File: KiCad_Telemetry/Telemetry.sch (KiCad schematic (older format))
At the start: 42 parts, among them J1 USB_A to Computer, J2 Conn_ARM_JTAG_SWD_10, J3 3.3 V Connectors, J5 5V Connectors, SW1 Reset Button, U1 NRF24L01_Breakout, U2 STM32F042C6T7, U3 AZ1117-3.3, Y1 8 MHz

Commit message: Initial STM32 project commit
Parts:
- removed D10, D11, D5, D6, D7, D8, D9: LED, symbol Device:LED
- removed R3, R4, R5, R6, R7, R8, R9: 65, symbol Device:R
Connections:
- wire segments 131 -> 110

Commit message: Updated the schematic
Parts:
- removed J2: Conn_ARM_JTAG_SWD_10, symbol Connector:Conn_ARM_JTAG_SWD_10
- removed U3: AZ1117-3.3, symbol Regulator_Linear:AZ1117-3.3
- removed U?: SN65HVD230, Package_SO:SOIC-8_3.9x4.9mm_P1.27mm, symbol Interface_CAN_LIN:SN65HVD230
- added C1: Opt. Decoupling Cap, Capacitor_SMD:C_0603_1608Metric_Pad1.05x0.95mm_HandSolder, symbol Device:C_Small
- added J2: Conn_01x05, Connector_PinHeader_2.54mm:PinHeader_1x05_P2.54mm_Vertical, symbol Connector_Generic:Conn_01x05
- added J6: Conn_01x07, symbol Connector_Generic:Conn_01x07
- added U3: TLV70033_SOT23-5, Package_TO_SOT_SMD:SOT-23-5, symbol Regulator_Linear:TLV70033_SOT23-5
- added U4: TPS7A7001DDA, Package_SO:TI_SO-PowerPAD-8, symbol Regulator_Linear:TPS7A7001DDA
- 0.1uF1, C2, C3, C4, C5, C7: footprint (none) -> Capacitor_SMD:C_0603_1608Metric_Pad1.05x0.95mm_HandSolder
- 100nF1: renamed from 100nF; footprint (none) -> Capacitor_SMD:C_0603_1608Metric_Pad1.05x0.95mm_HandSolder
- C6: value 22uF -> 1uF; footprint (none) -> Capacitor_SMD:C_0603_1608Metric_Pad1.05x0.95mm_HandSolder
- C8: value 10uF -> 1uF; footprint (none) -> Capacitor_SMD:C_0603_1608Metric_Pad1.05x0.95mm_HandSolder
- D1, D2: footprint (none) -> LED_SMD:LED_0603_1608Metric_Pad1.05x0.95mm_HandSolder
- D3, D4: footprint (none) -> Diode_SMD:D_0603_1608Metric_Pad1.05x0.95mm_HandSolder
- J1: footprint (none) -> Connector_USB:USB_A_CNCTech_1001-011-01101_Horizontal; MouserNO (none) -> 530-SS-52100-001; UnitPrice (none) -> 0,387
- R1, R2: footprint (none) -> Resistor_SMD:R_0603_1608Metric_Pad1.05x0.95mm_HandSolder
- R3, R4: renamed from R?; footprint (none) -> Resistor_SMD:R_0603_1608Metric_Pad1.05x0.95mm_HandSolder
- U2: footprint (none) -> Package_QFP:LQFP-48-1EP_7x7mm_P0.5mm_EP3.6x3.6mm; MouserNO (none) -> 511-STM32F042C6T7; UnitPrice (none) -> 2,75
- Y1: footprint (none) -> Crystal:Crystal_HC49-4H_Vertical
- gave numbers to parts that had none: 1
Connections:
- wire segments 110 -> 123
- no-connect marks 23 -> 20
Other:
- note added: "Determine CAN IC"
- note added: "Possibly peak 48 Volt input voltage rail in car"
- note added: "Unable to design solution until Mechanical choose Tires\n\nCurrent solution: SPI Connection for external board, similar to the NRF24"
- note removed: "2.4 GHZ or 433 MHz ?"
- note removed: "3.3V Rail; Stable or not? How do we reduce voltage ripple?"
- note removed: "Determine IC for this"
- note removed: "Does the car already have a solution?"
- note removed: "FSK?"
- note removed: "Suggested solution:\n- Purchase TPMS solution for wheels\n- Spy with RTLSDR\n- Purchase receiver module with demodulation\n- Fit on to board."
- note removed: "What Modulation is used?"
- moved on the sheet: C6

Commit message: Completed footprint allocation and BOM
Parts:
- removed R3, R4: R, Resistor_SMD:R_0603_1608Metric_Pad1.05x0.95mm_HandSolder, symbol Device:R
- removed SW1: Reset Button, symbol Switch:SW_Push
- removed U4: TPS7A7001DDA, Package_SO:TI_SO-PowerPAD-8, symbol Regulator_Linear:TPS7A7001DDA
- added C10: Opt. Decoupling Cap, Capacitor_SMD:C_0603_1608Metric_Pad1.05x0.95mm_HandSolder, symbol Device:C_Small
- added IC1: TCAN1044VDRQ1, SOIC127P600X175-8N, symbol TCAN1044VDRQ1:TCAN1044VDRQ1
- added S1: B3F-4000, B3F-4000, symbol B3F-4000:B3F-4000
- C11: renamed from 0.1uF1; value C_Small -> 0.1 uF
- C9: renamed from 100nF1; value C_Small -> 100nF
- D1, D2: MouserNO (none) -> 720-KRDELPS122A5163; UnitPrice (none) -> 0,369 €
- J1: Description (none) -> USB Connection for 5V Supply and PC Communication
- J3, J4, J5: footprint (none) -> TerminalBlock_Phoenix:TerminalBlock_Phoenix_MKDS-1,5-2_1x02_P5.00mm_Horizontal; MouserNO (none) -> 651-1934861; UnitPrice (none) -> 0,387 €
- J6: footprint (none) -> Connector_PinSocket_1.00mm:PinSocket_1x07_P1.00mm_Vertical
- R1: value 65 -> 55
- R2: value R -> 55
- U1: Description (none) -> NRF24 Breakout board connection: Board purchased seperately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
- U2: Description (none) -> STM32 Processor; USB, CAN, UART, SPI Comms.
- U3: Description (none) -> 5V to 3.3V Linear regulator
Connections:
- net labels added: CAN_STB
- wire segments 123 -> 129
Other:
- note added: "All LED's assume Vf = 2.2 V , If = 20 mA"
- note removed: "All LED's assume Vf = 2 V , If = 20 mA"
- note removed: "Determine CAN IC"
- note removed: "IS CAN 5V or 3.3 V?"
- moved on the sheet: C11, J4, J5

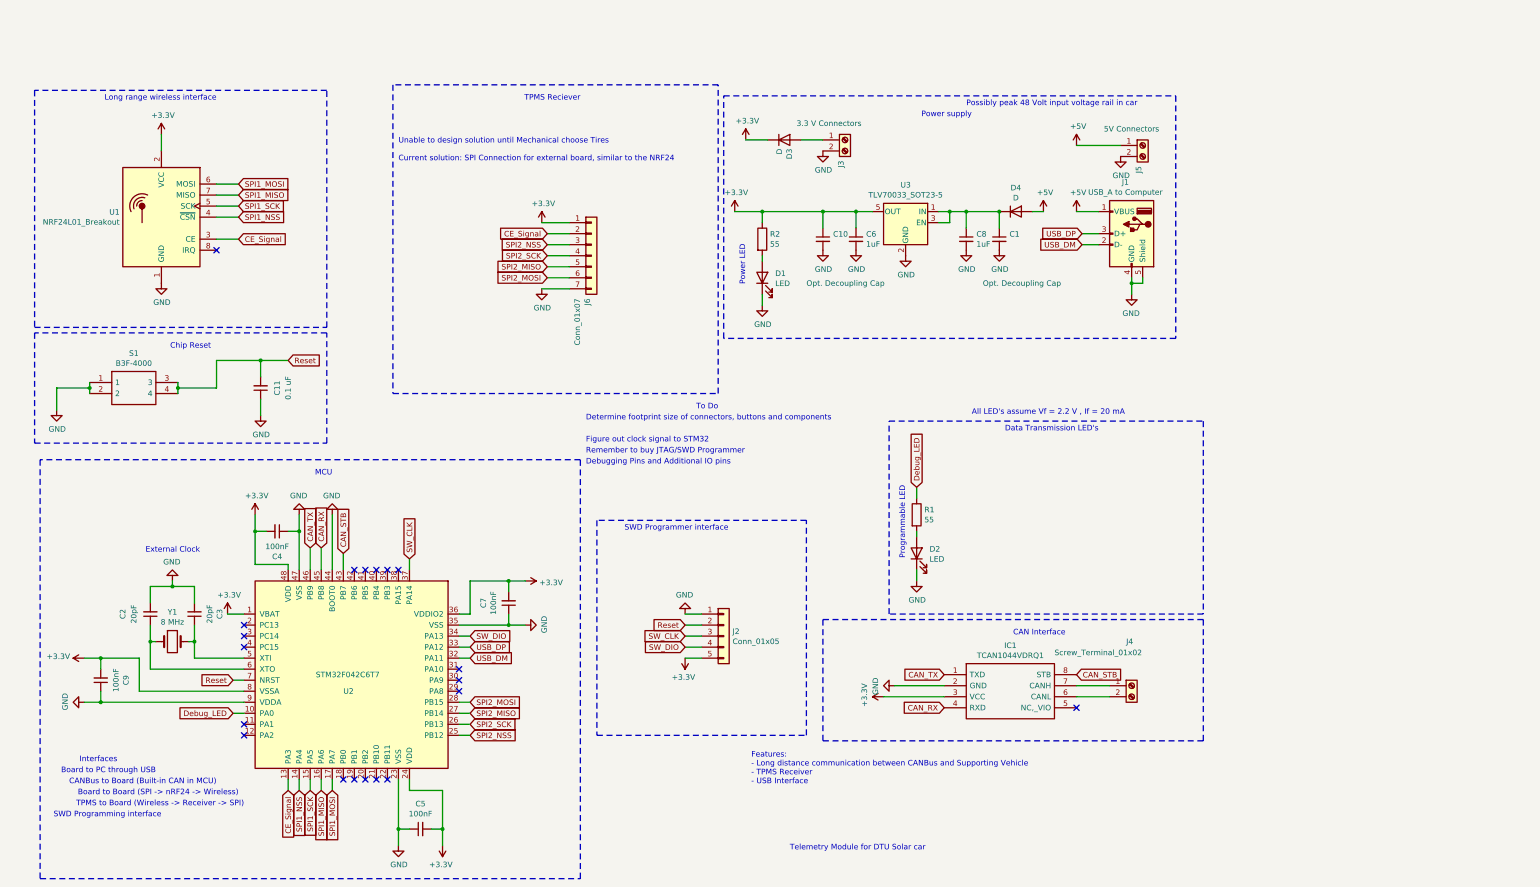
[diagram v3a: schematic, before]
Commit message: Finished intial CAN-FD KiCad Design. Awaiting peer review
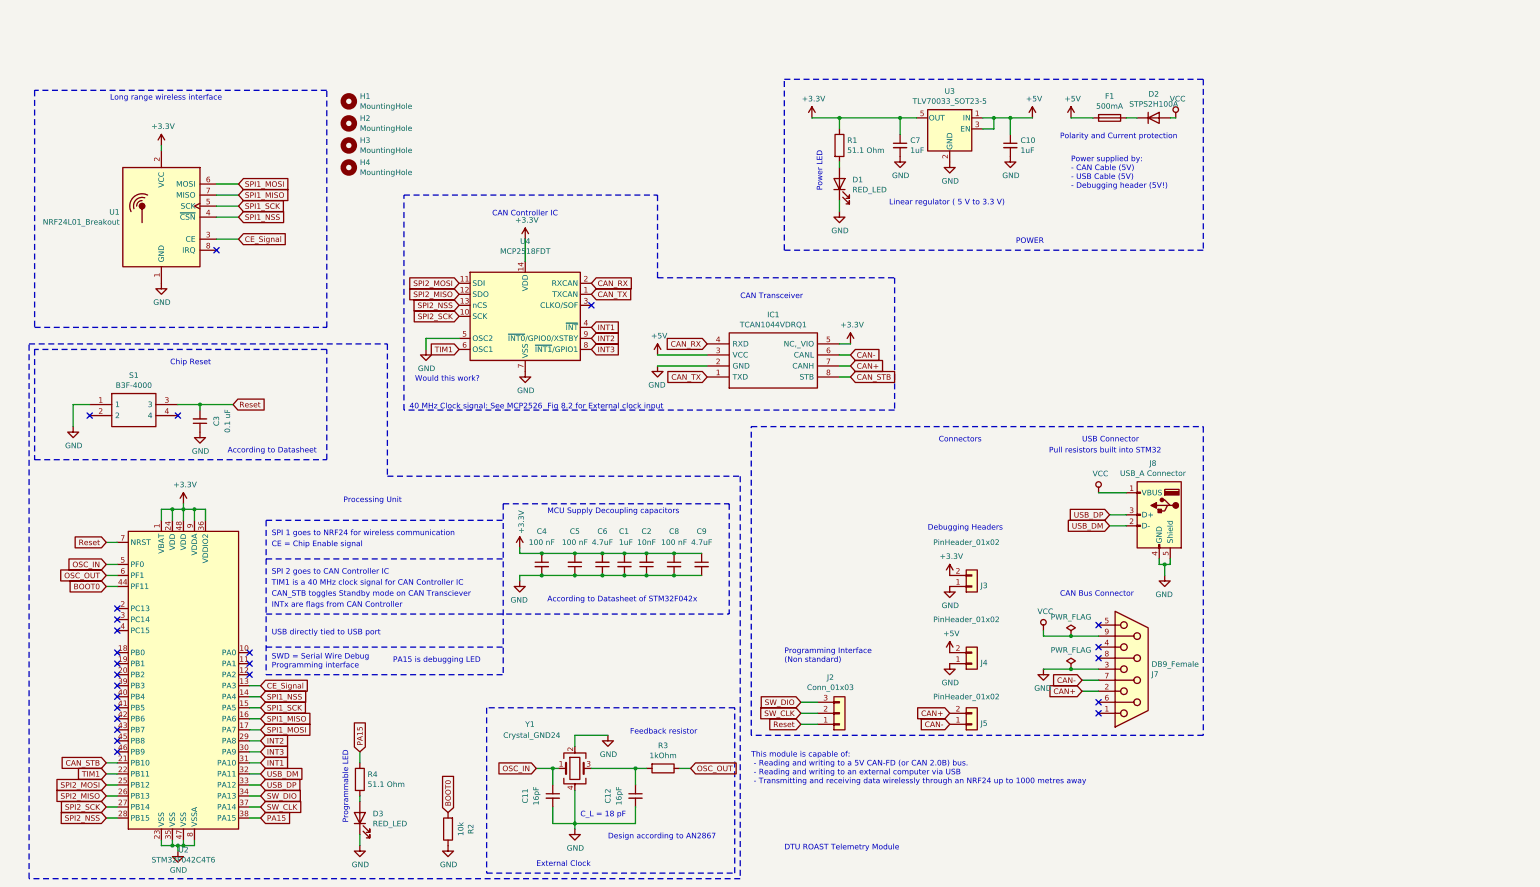
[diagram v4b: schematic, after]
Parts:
- removed C2, C3: 20pF, Capacitor_SMD:C_0603_1608Metric_Pad1.05x0.95mm_HandSolder, symbol Device:C_Small
- removed D3: D, Diode_SMD:D_0603_1608Metric_Pad1.05x0.95mm_HandSolder, symbol Device:D
- removed J2: Conn_01x05, Connector_PinHeader_2.54mm:PinHeader_1x05_P2.54mm_Vertical, symbol Connector_Generic:Conn_01x05
- removed J3: 3.3 V Connectors, TerminalBlock_Phoenix:TerminalBlock_Phoenix_MKDS-1,5-2_1x02_P5.00mm_Horizontal, symbol Connector:Screw_Terminal_01x02
- removed J4: Screw_Terminal_01x02, TerminalBlock_Phoenix:TerminalBlock_Phoenix_MKDS-1,5-2_1x02_P5.00mm_Horizontal, symbol Connector:Screw_Terminal_01x02
- removed J5: 5V Connectors, TerminalBlock_Phoenix:TerminalBlock_Phoenix_MKDS-1,5-2_1x02_P5.00mm_Horizontal, symbol Connector:Screw_Terminal_01x02
- removed J6: Conn_01x07, Connector_PinSocket_1.00mm:PinSocket_1x07_P1.00mm_Vertical, symbol Connector_Generic:Conn_01x07
- removed U2: STM32F042C6T7, Package_QFP:LQFP-48-1EP_7x7mm_P0.5mm_EP3.6x3.6mm, symbol stm32f042c6t7:STM32F042C6T7
- removed Y1: 8 MHz, Crystal:Crystal_HC49-4H_Vertical, symbol Device:Crystal
- added C11, C12: 16pF, Capacitor_SMD:C_0402_1005Metric, symbol Device:C_Small
- added C9: 4.7uF, Capacitor_SMD:C_0402_1005Metric, symbol Device:C_Small
- added F1: 500mA, Fuse:Fuse_0603_1608Metric_Pad1.05x0.95mm_HandSolder, symbol Device:Fuse
- added H1, H2, H3, H4: MountingHole, MountingHole:MountingHole_3.5mm, symbol Mechanical:MountingHole
- added J2: Conn_01x03, Connector_PinHeader_2.54mm:PinHeader_1x03_P2.54mm_Vertical, symbol Connector_Generic:Conn_01x03
- added J3, J4, J5: PinHeader_01x02, Connector_PinHeader_2.54mm:PinHeader_1x02_P2.54mm_Vertical, symbol Connector_Generic:Conn_01x02
- added J7: DB9_Female, Connector_Dsub:DSUB-9_Female_Horizontal_P2.77x2.84mm_EdgePinOffset4.94mm_Housed_MountingHolesOffset7.48mm, symbol Connector:DB9_Female
- added R3: 1kOhm, Resistor_SMD:R_0402_1005Metric, symbol Device:R
- added R4: 51.1 Ohm, Resistor_SMD:R_0603_1608Metric_Pad1.05x0.95mm_HandSolder, symbol Device:R
- added U2: STM32F042C4T6, Package_QFP:LQFP-48_7x7mm_P0.5mm, symbol MCU_ST_STM32F0:STM32F042C4Tx
- added U4: MCP2518FDT, Package_SO:SOIC-14_3.9x8.7mm_P1.27mm, symbol Interface_CAN_LIN:MCP2517FD-xSL
- added Y1: Crystal_GND24, Crystal:Crystal_SMD_Abracon_ABM3B-4Pin_5.0x3.2mm, symbol Device:Crystal_GND24
- C1: value Opt. Decoupling Cap -> 1uF; footprint Capacitor_SMD:C_0603_1608Metric_Pad1.05x0.95mm_HandSolder -> Capacitor_SMD:C_0402_1005Metric; Description (none) -> Supply cap for STM32; MouserNO (none) -> 81-GRT155R61E105KE1D; UnitPrice (none) -> 0,153
- C10: value Opt. Decoupling Cap -> 1uF; footprint Capacitor_SMD:C_0603_1608Metric_Pad1.05x0.95mm_HandSolder -> Capacitor_SMD:C_0402_1005Metric; Description (none) -> X5R Low ESR Cap for stable Voltage regulation; MouserNO (none) -> 81-GRT155R61E105KE1D; UnitPrice (none) -> 0,153
- C2: renamed from C9; value 100nF -> 10nF; footprint Capacitor_SMD:C_0603_1608Metric_Pad1.05x0.95mm_HandSolder -> Capacitor_SMD:C_0402_1005Metric; Description (none) -> Supply voltage cap; MouserNO (none) -> 80-C0402C103J3RAUTO; UnitPrice (none) -> 0,099
- C3: renamed from C11; footprint Capacitor_SMD:C_0603_1608Metric_Pad1.05x0.95mm_HandSolder -> Capacitor_SMD:C_0402_1005Metric; Description (none) -> Reset Cap to combat parasitic resets (According to Datashee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; MouserNO (none) -> 81-GRM155C71H104JE9D; UnitPrice (none) -> 0,09
- C4, C5: value 100nF -> 100 nF; footprint Capacitor_SMD:C_0603_1608Metric_Pad1.05x0.95mm_HandSolder -> Capacitor_SMD:C_0402_1005Metric; Description (none) -> Supply cap for STM32; MouserNO (none) -> 81-GRM155C71H104JE9D; UnitPrice (none) -> 0,09
- C6: value 1uF -> 4.7uF; footprint Capacitor_SMD:C_0603_1608Metric_Pad1.05x0.95mm_HandSolder -> Capacitor_SMD:C_0402_1005Metric; Description (none) -> Supply caps for STM32; MouserNO (none) -> 603-CC0402KR5R6BB475; UnitPrice (none) -> 0,126
- C7: value 100nF -> 1uF; footprint Capacitor_SMD:C_0603_1608Metric_Pad1.05x0.95mm_HandSolder -> Capacitor_SMD:C_0402_1005Metric; Description (none) -> X5R Low ESR Cap for stable Voltage regulation; MouserNO (none) -> 81-GRT155R61E105KE1D; UnitPrice (none) -> 0,153
- C8: value 1uF -> 100 nF; footprint Capacitor_SMD:C_0603_1608Metric_Pad1.05x0.95mm_HandSolder -> Capacitor_SMD:C_0402_1005Metric; Description (none) -> Supply cap for STM32; MouserNO (none) -> 81-GRM155C71H104JE9D; UnitPrice (none) -> 0,09
- D1: value LED -> RED_LED; Description (none) -> RED LED to indicate power ON; UnitPrice 0,369 € -> 0,369
- D2: renamed from D4; value D -> STPS2H100A; footprint Diode_SMD:D_0603_1608Metric_Pad1.05x0.95mm_HandSolder -> Diode_SMD:D_SMA_Handsoldering; Description (none) -> Supply voltage polarity protection diode; MouserNO (none) -> 511-STPS2H100A; UnitPrice (none) -> 0,414
- D3: renamed from D2; value LED -> RED_LED; Description (none) -> Programmable LED to enable software debugging through Blink; MouserNO 720-KRDELPS122A5163 -> 720-KRDELPS122A5163; UnitPrice 0,369 € -> 0,369
- IC1: footprint SOIC127P600X175-8N -> Package_SO:SOIC-8_3.9x4.9mm_P1.27mm; Height 1.75 -> (none); Manufacturer_Name Texas Instruments -> (none); Manufacturer_Part_Number TCAN1044VDRQ1 -> (none); MouserNO 595-TCAN1044VDRQ1 -> 595-TCAN1044VDRQ1; UnitPrice https://www.mouser.com/Search/Refine.aspx?Keyword=595-TCAN1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 -> 1,13
- J8: renamed from J1; value USB_A to Computer -> USB_A Connector; footprint Connector_USB:USB_A_CNCTech_1001-011-01101_Horizontal -> Connector_USB:USB_A_Stewart_SS-52100-001_Horizontal; UnitPrice 0,387 -> 0.387
- R1: value 55 -> 51.1 Ohm; Description (none) -> LED Current limiting resistor; MouserNO (none) -> 754-RR0816Q-51R1D69R; UnitPrice (none) -> 0,09
- R2: value 55 -> 10k; Description (none) -> Pull down resistor to disable bootloader (can be shorted); MouserNO (none) -> 754-RR0816P-912D; UnitPrice (none) -> 0,09
- S1: footprint B3F-4000 -> B3F-4000:B3F-4000; Height (none) -> 4mm
- U1: footprint RF_Module:nRF24L01_Breakout -> mysensors_radios:NRF24L01PALNA_THT; MouserNO (none) -> None; UnitPrice (none) -> 70 kr
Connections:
- net Debug_LED is gone; now on net +3V3: R1.1
- net +3V3: now also C1.1, C4.1, C6.2, C7.1, C8.1, IC1.5 (NC,_VIO), C9.1, J3.2 (Pin_2), U2.1 (VBAT), U2.24 (VDD), U2.36 (VDDIO2), U2.48 (VDD), U2.9 (VDDA), U4.14 (VDD); no longer C10.1, C4.2, C6.1, C7.2, IC1.3 (VCC), R2.1
- net +5V: now also C10.1, IC1.3 (VCC), U3.1 (IN), U3.3 (EN), F1.2, J4.2 (Pin_2); no longer D2.2 (A), J8.1 (VBUS)
- net CAN_RX: now also U4.2 (RXCAN)
- net CAN_STB: now also U2.21 (PB10)
- net CAN_TX: now also U4.1 (TXCAN)
- net CE_Signal: now also U2.13 (PA3)
- net GND: now also C4.2, C6.1, C7.2, R2.1, C11.2, C12.2, C9.2, J3.1 (Pin_1), J4.1 (Pin_1), J7.3, U2.23 (VSS), U2.35 (VSS), U2.47 (VSS), U2.8 (VSSA), U4.5 (OSC2), U4.7 (VSS), Y1.2, Y1.4; no longer C4.1, C6.2, C7.1, S1.2
- net Reset: now also J2.1 (Pin_1), U2.7 (NRST); no longer S1.4
- net SPI1_MISO: now also U2.16 (PA6)
- net SPI1_MOSI: now also U2.17 (PA7)
- net SPI1_NSS: now also U2.14 (PA4)
- net SPI1_SCK: now also U2.15 (PA5)
- net SPI2_MISO: now also U2.26 (PB13), U4.12 (SDO)
- net SPI2_MOSI: now also U2.25 (PB12), U4.11 (SDI)
- net SPI2_NSS: now also U2.28 (PB15), U4.13 (nCS)
- net SPI2_SCK: now also U2.27 (PB14), U4.10 (SCK)
- net SW_CLK: now also J2.2 (Pin_2), U2.37 (PA14)
- net SW_DIO: now also J2.3 (Pin_3), U2.34 (PA13)
- net USB_DM: now also U2.32 (PA11)
- net USB_DP: now also U2.33 (PA12)
- net at D1.2 (A): now also R1.2; no longer R2.2
- net at D3.2 (A): now also R4.2; no longer R1.2
- net CAN+: now reaches IC1.7 (CANH)
- net CAN+: now also J5.2 (Pin_2), J7.2
- net CAN-: now reaches IC1.6 (CANL)
- net CAN-: now also J5.1 (Pin_1), J7.7
- new net: D2.1 (K), F1.1
- new net: C12.1, R3.2, Y1.3
- new net BOOT0: R2.2, U2.44 (PF11)
- new net INT1: U2.31 (PA10), U4.4 (~INT)
- new net INT2: U2.29 (PA8), U4.9 (~INT0~/GPIO0/XSTBY)
- new net INT3: U2.30 (PA9), U4.8 (~INT1~/GPIO1)
- new net OSC_IN: C11.1, U2.5 (PF0), Y1.1
- new net OSC_OUT: R3.1, U2.6 (PF1)
- new net PA15: R4.1, U2.38 (PA15)
- new net TIM1: U2.22 (PB11), U4.6 (OSC1)
- new net VCC: D2.2 (A), J7.9, J8.1 (VBUS)
- no-connect marks 20 -> 25
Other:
- note added: "40 MHz Clock signal: See MCP2526 Fig 8.2 for External clock input"
- note added: "According to Datasheet"
- note added: "According to Datasheet of STM32F042x"
- note added: "CAN Bus Connector"
- note added: "CAN Controller IC"
- note added: "CAN Transceiver"
- note added: "CAN_STB toggles Standby mode on CAN Transciever"
- note added: "CE = Chip Enable signal"
- note added: "C_L = 18 pF"
- note added: "Connectors"
- note added: "DTU ROAST Telemetry Module"
- note added: "Debugging Headers"
- note added: "Design according to AN2867"
- note added: "Feedback resistor"
- note added: "INTx are flags from CAN Controller"
- note added: "Linear regulator ( 5 V to 3.3 V)"
- note added: "MCU Supply Decoupling capacitors"
- note added: "PA15 is debugging LED"
- note added: "POWER"
- note added: "Polarity and Current protection"
- note added: "Power supplied by:\n- CAN Cable (5V)\n- USB Cable (5V)\n- Debugging header (5V!)"
- note added: "Processing Unit"
- note added: "Programming Interface \n(Non standard)"
- note added: "Pull resistors built into STM32"
- note added: "SPI 1 goes to NRF24 for wireless communication"
- note added: "SPI 2 goes to CAN Controller IC"
- note added: "SWD = Serial Wire Debug\nProgramming interface"
- note added: "TIM1 is a 40 MHz clock signal for CAN Controller IC"
- note added: "This module is capable of:\n - Reading and writing to a 5V CAN-FD (or CAN 2.0B) bus.\n - Reading and writing to an external computer via USB\n - Transmitting and receiving data wirelessly through an NRF24 up to 1000 metres away"
- note added: "USB Connector"
- note added: "USB directly tied to USB port"
- note added: "Would this work?"
- note removed: "All LED's assume Vf = 2.2 V , If = 20 mA"
- note removed: "Board to Board (SPI -> nRF24 -> Wireless)"
- note removed: "Board to PC through USB"
- note removed: "CAN Interface"
- note removed: "CANBus to Board (Built-in CAN in MCU)"
- note removed: "Data Transmission LED's"
- note removed: "Debugging Pins and Additional IO pins"
- note removed: "Determine footprint size of connectors, buttons and components"
- note removed: "Features:\n- Long distance communication between CANBus and Supporting Vehicle\n- TPMS Receiver\n- USB Interface"
- note removed: "Figure out clock signal to STM32"
- note removed: "Interfaces"
- note removed: "MCU"
- note removed: "Possibly peak 48 Volt input voltage rail in car"
- note removed: "Power supply"
- note removed: "Remember to buy JTAG/SWD Programmer\n"
- note removed: "SWD Programmer interface"
- note removed: "SWD Programming interface"
- note removed: "TPMS Reciever"
- note removed: "TPMS to Board (Wireless -> Receiver -> SPI)"
- note removed: "Telemetry Module for DTU Solar car"
- note removed: "To Do\n"
- note removed: "Unable to design solution until Mechanical choose Tires\n\nCurrent solution: SPI Connection for external board, similar to the NRF24"
- moved on the sheet: C2, C3, D2, D3, J8, S1, U3
